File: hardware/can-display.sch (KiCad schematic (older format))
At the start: 31 parts, among them J1 Conn_01x10_Female, J2 Conn_02x09_Odd_Even, J3 Conn_01x04_Male, J4 Conn_01x02_Male, J5 Conn_01x04_Male, J6 Conn_01x04_Male, U1 STM32F446RCTx, U2 MCP4019, U3 TLC59284, U4 MCP2562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

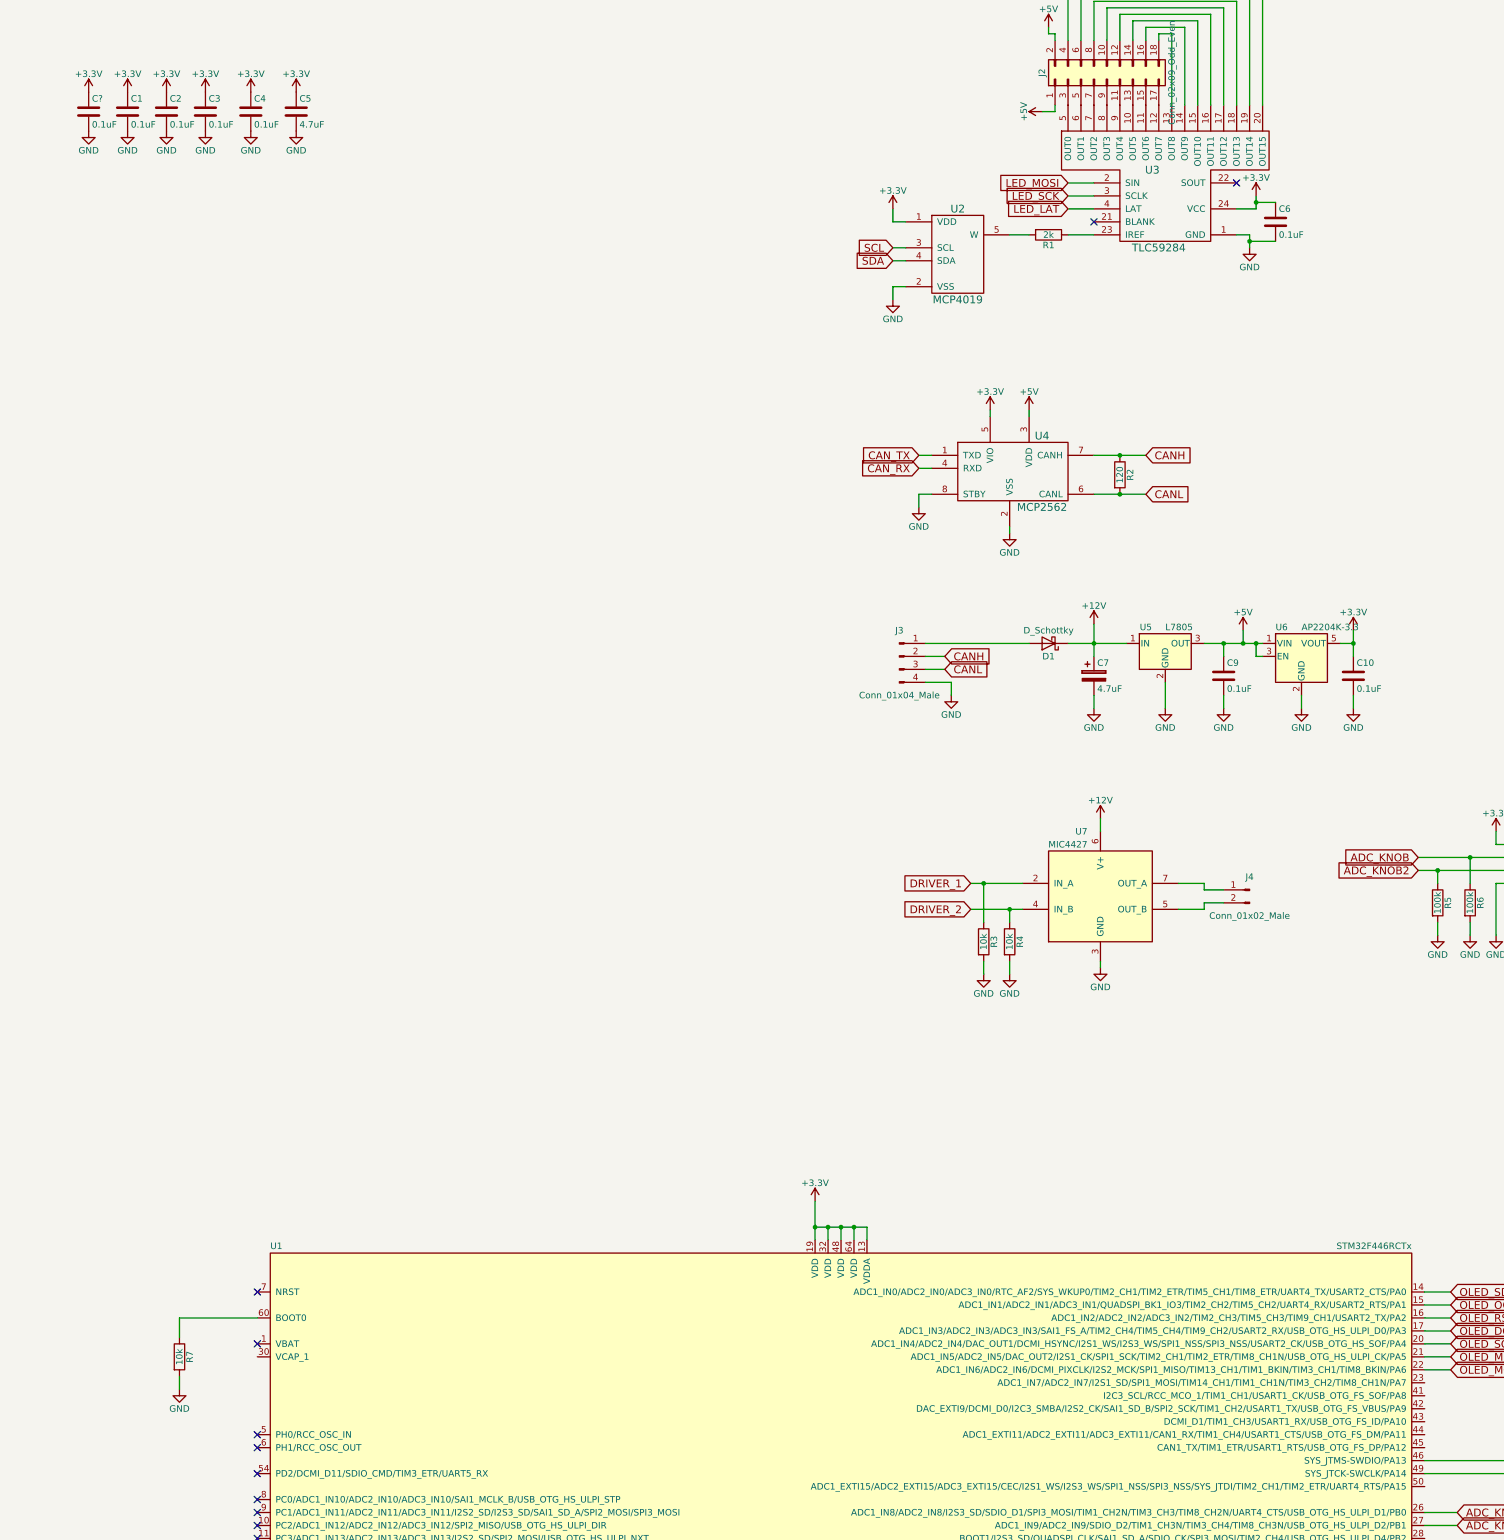
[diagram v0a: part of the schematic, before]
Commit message: Switch to F336RET6
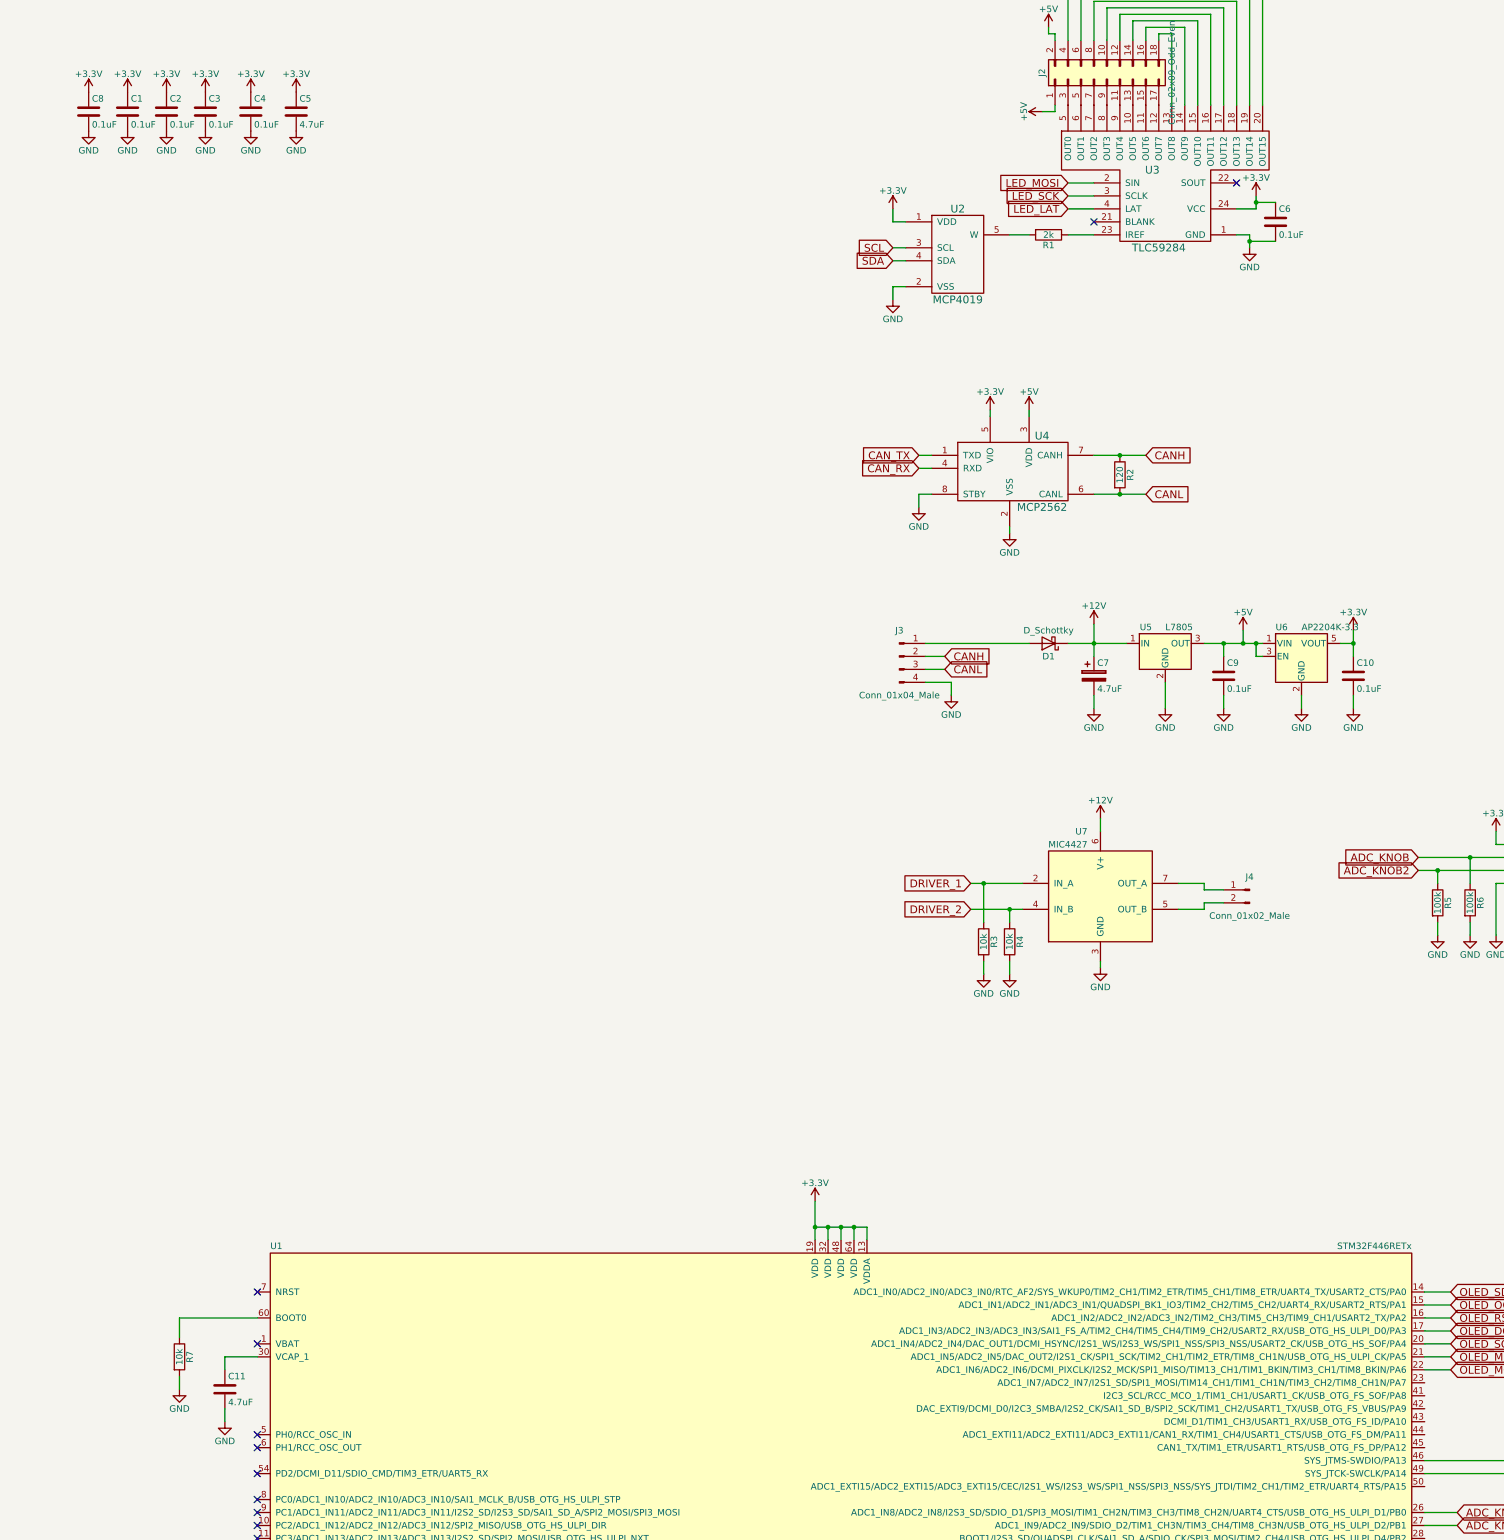
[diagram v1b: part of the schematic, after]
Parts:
- removed U1: STM32F446RCTx, Housings_QFP:LQFP-64_10x10mm_Pitch0.5mm, symbol STM32F446RCTx
- added C11: 4.7uF, Capacitors_SMD:C_0603, symbol C
- added U1: STM32F446RETx, Housings_QFP:LQFP-64_10x10mm_Pitch0.5mm, symbol STM32F446RETx
- gave numbers to parts that had none: 1
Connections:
- net +3V3: now also U1.13 (VDDA), U1.19 (VDD), U1.32 (VDD), U1.48 (VDD), U1.64 (VDD)
- net ADC_KNOB: now also U1.26 (ADC1_IN8/ADC2_IN8/I2S3_SD/SDIO_D1/SPI3_MOSI/TIM1_CH2N/TIM3_CH3/TIM8_CH2N/UART4_CTS/USB_OTG_HS_ULPI_D1/PB0)
- net ADC_KNOB2: now also U1.27 (ADC1_IN9/ADC2_IN9/SDIO_D2/TIM1_CH3N/TIM3_CH4/TIM8_CH3N/USB_OTG_HS_ULPI_D2/PB1)
- net CAN_RX: now also U1.61 (CAN1_RX/DCMI_D6/I2C1_SCL/SDIO_D4/TIM10_CH1/TIM2_CH1/TIM2_ETR/TIM4_CH3/PB8)
- net CAN_TX: now also U1.62 (CAN1_TX/DAC_EXTI9/DCMI_D7/I2C1_SDA/I2S2_WS/SAI1_FS_B/SDIO_D5/SPI2_NSS/TIM11_CH1/TIM2_CH2/TIM4_CH4/PB9)
- net DRIVER_1: now also U1.55 (I2C2_SDA/I2S1_CK/I2S3_CK/SPI1_SCK/SPI3_SCK/SYS_JTDO-SWO/TIM2_CH2/PB3)
- net DRIVER_2: now also U1.56 (I2C3_SDA/I2S2_WS/SPI1_MISO/SPI2_NSS/SPI3_MISO/SYS_JTRST/TIM3_CH1/PB4)
- net GND: now also C11.2, U1.12 (VSSA), U1.18 (VSS), U1.31 (VSS), U1.47 (VSS), U1.63 (VSS)
- net LED_LAT: now also U1.33 (CAN2_RX/I2C2_SMBA/I2S2_WS/SAI1_SCK_B/SPI2_NSS/TIM1_BKIN/USART3_CK/USB_OTG_HS_ID/USB_OTG_HS_ULPI_D5/PB12)
- net LED_MOSI: now also U1.36 (ADC1_EXTI15/ADC2_EXTI15/ADC3_EXTI15/I2S2_SD/RTC_REFIN/SPI2_MOSI/TIM12_CH2/TIM1_CH3N/TIM8_CH3N/USB_OTG_HS_DP/PB15)
- net LED_SCK: now also U1.34 (CAN2_TX/I2S2_CK/SPI2_SCK/TIM1_CH1N/USART3_CTS/USB_OTG_HS_ULPI_D6/USB_OTG_HS_VBUS/PB13)
- net OLED_DC: now also U1.17 (ADC1_IN3/ADC2_IN3/ADC3_IN3/SAI1_FS_A/TIM2_CH4/TIM5_CH4/TIM9_CH2/USART2_RX/USB_OTG_HS_ULPI_D0/PA3)
- net OLED_MISO: now also U1.21 (ADC1_IN5/ADC2_IN5/DAC_OUT2/I2S1_CK/SPI1_SCK/TIM2_CH1/TIM2_ETR/TIM8_CH1N/USB_OTG_HS_ULPI_CK/PA5)
- net OLED_MOSI: now also U1.22 (ADC1_IN6/ADC2_IN6/DCMI_PIXCLK/I2S2_MCK/SPI1_MISO/TIM13_CH1/TIM1_BKIN/TIM3_CH1/TIM8_BKIN/PA6)
- net OLED_OCS: now also U1.15 (ADC1_IN1/ADC2_IN1/ADC3_IN1/QUADSPI_BK1_IO3/TIM2_CH2/TIM5_CH2/UART4_RX/USART2_RTS/PA1)
- net OLED_RST: now also U1.16 (ADC1_IN2/ADC2_IN2/ADC3_IN2/TIM2_CH3/TIM5_CH3/TIM9_CH1/USART2_TX/PA2)
- net OLED_SCK: now also U1.20 (ADC1_IN4/ADC2_IN4/DAC_OUT1/DCMI_HSYNC/I2S1_WS/I2S3_WS/SPI1_NSS/SPI3_NSS/USART2_CK/USB_OTG_HS_SOF/PA4)
- net OLED_SDCS: now also U1.14 (ADC1_IN0/ADC2_IN0/ADC3_IN0/RTC_AF2/SYS_WKUP0/TIM2_CH1/TIM2_ETR/TIM5_CH1/TIM8_ETR/UART4_TX/USART2_CTS/PA0)
- net SCL: now also U1.58 (CAN2_TX/CEC/DCMI_D5/I2C1_SCL/QUADSPI_BK1_NCS/TIM4_CH1/USART1_TX/PB6)
- net SDA: now also U1.59 (DCMI_VSYNC/I2C1_SDA/SPDIFRX_IN0/TIM4_CH2/USART1_RX/PB7)
- net at J6.2 (Pin_2): now also U1.49 (SYS_JTCK-SWCLK/PA14)
- net at J6.4 (Pin_4): now also U1.46 (SYS_JTMS-SWDIO/PA13)
- net at R7.1: now also U1.60 (BOOT0)
- new net: C11.1, U1.30 (VCAP_1)
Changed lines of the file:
@@
 Wire Wire Line
 	16400 9950 16600 9950
-$Comp
-L STM32F446RCTx U1
-U 1 1 5AC6F7DE
-P 11900 11550
-F 0 "U1" H 7500 13475 50  0000 L BNN
-F 1 "STM32F446RCTx" H 16300 13475 50  0000 R BNN
-F 2 "Housings_QFP:LQFP-64_10x10mm_Pitch0.5mm" H 16300 13425 50  0001 R TNN
-F 3 "" H 11900 11550 50  0001 C CNN
-	1    11900 11550
-	1    0    0    -1
-$EndComp
 Wire Wire Line
 	12100 9450 12100 9550
@@
 NoConn ~ 7400 12250
 $Comp
-L C C?
+L C C8
 U 1 1 5AC72FE5
 P 6100 850
-F 0 "C?" H 6125 950 50  0000 L CNN
+F 0 "C8" H 6125 950 50  0000 L CNN
 F 1 "0.1uF" H 6125 750 50  0000 L CNN
 F 2 "Capacitors_SMD:C_0603" H 6138 700 50  0001 C CNN
@@
 $EndComp
 $Comp
-L +3.3V #PWR?
+L +3.3V #PWR045
 U 1 1 5AC72FEB
 P 6100 700
-F 0 "#PWR?" H 6100 550 50  0001 C CNN
+F 0 "#PWR045" H 6100 550 50  0001 C CNN
 F 1 "+3.3V" H 6100 840 50  0000 C CNN
 F 2 "" H 6100 700 50  0001 C CNN
@@
 $EndComp
 $Comp
-L GND #PWR?
+L GND #PWR046
 U 1 1 5AC72FF1
 P 6100 1000
-F 0 "#PWR?" H 6100 750 50  0001 C CNN
+F 0 "#PWR046" H 6100 750 50  0001 C CNN
 F 1 "GND" H 6100 850 50  0000 C CNN
 F 2 "" H 6100 1000 50  0001 C CNN
@@
 	1    0    0    -1
 $EndComp
+$Comp
+L C C11
+U 1 1 5AC71785
+P 7150 10700
+F 0 "C11" H 7175 10800 50  0000 L CNN
+F 1 "4.7uF" H 7175 10600 50  0000 L CNN
+F 2 "Capacitors_SMD:C_0603" H 7188 10550 50  0001 C CNN
+F 3 "" H 7150 10700 50  0001 C CNN
+	1    7150 10700
+	1    0    0    -1
+$EndComp
+$Comp
+L GND #PWR047
+U 1 1 5AC71B4B
+P 7150 10950
+F 0 "#PWR047" H 7150 10700 50  0001 C CNN
+F 1 "GND" H 7150 10800 50  0000 C CNN
+F 2 "" H 7150 10950 50  0001 C CNN
+F 3 "" H 7150 10950 50  0001 C CNN
+	1    7150 10950
+	1    0    0    -1
+$EndComp
+Wire Wire Line
+	7150 10950 7150 10850
+Wire Wire Line
+	7150 10550 7150 10450
+Wire Wire Line
+	7150 10450 7400 10450
+$Comp
+L STM32F446RETx U1
+U 1 1 5AC72290
+P 11900 11550
+F 0 "U1" H 7500 13475 50  0000 L BNN
+F 1 "STM32F446RETx" H 16300 13475 50  0000 R BNN
+F 2 "Housings_QFP:LQFP-64_10x10mm_Pitch0.5mm" H 16300 13425 50  0001 R TNN
+F 3 "" H 11900 11550 50  0001 C CNN
+	1    11900 11550
+	1    0    0    -1
+$EndComp

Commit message: Add i2c resistors
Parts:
- added R8, R9: 4.7k, Resistors_SMD:R_0603, symbol R
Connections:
- net +3V3: now also R8.2, R9.2
- net SCL: now also R8.1
- net SDA: now also R9.1

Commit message: switch to f429
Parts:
- removed U1: STM32F446RETx, Housings_QFP:LQFP-64_10x10mm_Pitch0.5mm, symbol STM32F446RETx
- added U?: STM32F429VITx, LQFP100, symbol STM32F429VITx
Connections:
- wire segments 155 -> 156
- no-connect marks 18 -> 5
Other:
- moved on the sheet: C11, J6, R7

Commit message: board almost final
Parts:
- added C12: 2.2uF, Capacitors_SMD:C_0603, symbol C
- added D2, D3, D4: LED, LEDs:LED_0603_HandSoldering, symbol LED
- added R10, R11, R12: 1k, Resistors_SMD:R_0603, symbol R
- C11: value 4.7uF -> 2.2uF
- U1: renamed from U?; footprint LQFP100 -> Housings_QFP:LQFP-100_14x14mm_Pitch0.5mm
- U4: footprint Housings_DFN_QFN:DFN-8-1EP_3x3mm_Pitch0.65mm -> Housings_SOIC:SOIC-8_3.9x4.9mm_Pitch1.27mm
- U7: footprint Housings_DFN_QFN:DFN-8-1EP_6x5mm_Pitch1.27mm_LargeFlag -> Housings_SOIC:SOIC-8_3.9x4.9mm_Pitch1.27mm
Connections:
- wire segments 156 -> 172
- no-connect marks 5 -> 70
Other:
- moved on the sheet: C11, R7
